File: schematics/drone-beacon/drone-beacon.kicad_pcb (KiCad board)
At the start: 2 copper layers, 23.3 x 29.9 mm, 13 parts, among them J1 ESP32 Flashing connector, J2 Power Input, SW1 Model selection, U1 ESP32-WROOM-32U, U2 AMS1117-3.3, U3 L80-R

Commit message: Update schematics
Signed-off-by: LAMBS Pierre-Antoine <pierreantoine.lambs@gmail.com>
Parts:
- C1, C2, C3, C4: footprint Capacitor_SMD:C_0201_0603Metric -> Capacitor_SMD:C_0402_1005Metric_Pad0.74x0.62mm_HandSolder
- D1: footprint LED_SMD:LED_0201_0603Metric -> LED_SMD:LED_0402_1005Metric_Pad0.77x0.64mm_HandSolder
- R1, R3: footprint Resistor_SMD:R_0201_0603Metric -> Resistor_SMD:R_0402_1005Metric_Pad0.72x0.64mm_HandSolder
- U3: value L80-R -> L96; footprint RF_GPS:Quectel_L96 -> QUECTEL_L96:L96
- moved D1 23.7 mm to (200.8, 51.9), turned to 90 degrees
- moved R1 21.7 mm to (200.8, 54.7), turned to 90 degrees
- moved R3 4.89 mm to (200.3, 72.5), turned to 0 degrees
- moved U3 0.42 mm to (190.8, 72.3)
- moved C2 0.21 mm to (190.8, 56.2)
- moved C3 0.13 mm to (196.9, 60.6)
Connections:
- U3 pad 1: /GPS_RX -> unconnected-(U3-NC1-Pad1)
- U3 pad 10: unconnected-(U3-~{RESET}-Pad10) -> GND
- U3 pad 11: unconnected-(U3-RESERVED-Pad11) -> GND
- U3 pad 13: (no net) -> GND
- U3 pad 14: (no net) -> GND
- U3 pad 15: (no net) -> GND
- U3 pad 16: (no net) -> unconnected-(U3-RF_OUT-Pad16)
- U3 pad 17: (no net) -> unconnected-(U3-RF_IN-Pad17)
- U3 pad 18: (no net) -> GND
- U3 pad 19: (no net) -> GND
- U3 pad 2: /GPS_TX -> unconnected-(U3-3D_FIX-Pad2)
- U3 pad 20: (no net) -> unconnected-(U3-JAM_DET-Pad20)
- U3 pad 21: (no net) -> GND
- U3 pad 22: (no net) -> GND
- U3 pad 23: (no net) -> +3.3V
- U3 pad 24: (no net) -> unconnected-(U3-GEO_FENCE-Pad24)
- U3 pad 25: (no net) -> /GPS_TX
- U3 pad 26: (no net) -> /GPS_RX
- U3 pad 27: (no net) -> GND
- U3 pad 28: (no net) -> unconnected-(U3-FORCE_ON-Pad28)
- U3 pad 29: (no net) -> /GPS_PPS
- U3 pad 3: GND -> unconnected-(U3-I2C_SDA-Pad3)
- U3 pad 30: (no net) -> unconnected-(U3-ANTON-Pad30)
- U3 pad 31: (no net) -> GND
- U3 pad 4: +3.3V -> GND
- U3 pad 5: unconnected-(U3-V_BCKP-Pad5) -> GND
- U3 pad 6: /GPS_PPS -> unconnected-(U3-I2C_SCL-Pad6)
- U3 pad 9: unconnected-(U3-NC-Pad9) -> +3.3V
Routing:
- net /GPS_PPS: track 18.3 -> 36.3 mm
- net +3.3V: track 51.3 -> 66.1 mm
- net /GPS_RX: track 13.4 -> 26.9 mm
- net /GPS_TX: track 14.6 -> 26.3 mm
- net /ESP32_EN: track 27.0 -> 32.3 mm
- net GND: track 4.50 -> 0.01 mm, vias 4 -> 3
- net /STATUS_LED: track 18.8 -> 21.4 mm
- net Net-(D1-K): track 0.80 -> 0.00 mm

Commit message: Update schematics (WIP)
Signed-off-by: LAMBS Pierre-Antoine <pierreantoine.lambs@gmail.com>
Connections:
- U1 pad 14: /DIP1 -> unconnected-(U1-IO12-Pad14)
- U1 pad 16: unconnected-(U1-IO13-Pad16) -> /DIP1
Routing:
- net /DIP1: track 21.9 -> 18.6 mm
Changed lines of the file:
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@@
 	(net 21 "unconnected-(U1-SHD{slash}SD2-Pad17)")
 	(net 22 "unconnected-(U1-IO33-Pad9)")
-	(net 23 "unconnected-(U1-IO13-Pad16)")
+	(net 23 "unconnected-(U1-IO12-Pad14)")
 	(net 24 "unconnected-(U1-IO18-Pad30)")
 	(net 25 "unconnected-(U1-IO5-Pad29)")
@@
 			(size 1.5 0.9)
 			(layers "F.Cu" "F.Mask" "F.Paste")
-			(net 10 "/DIP1")
+			(net 23 "unconnected-(U1-IO12-Pad14)")
 			(pinfunction "IO12")
-			(pintype "bidirectional")
+			(pintype "bidirectional+no_connect")
 		)
 		(pad "15" smd rect
@@
 			(size 1.5 0.9)
 			(layers "F.Cu" "F.Mask" "F.Paste")
-			(net 23 "unconnected-(U1-IO13-Pad16)")
+			(net 10 "/DIP1")
 			(pinfunction "IO13")
-			(pintype "bidirectional+no_connect")
+			(pintype "bidirectional")
 		)
 		(pad "17" smd rect
@@
 	)
 	(segment
-		(start 199.8 53.15)
-		(end 194.15 53.15)
+		(start 194.15 53.15)
+		(end 195.236 53.15)
+		(width 0.2)
+		(layer "F.Cu")
+		(net 10)
+	)
+	(segment
+		(start 195.236 53.15)
+		(end 195.495 52.891)
 		(width 0.2)
 		(layer "F.Cu")
@@
 		(width 0.2)
 		(layer "F.Cu")
+		(net 10)
+	)
+	(segment
+		(start 195.495 52.891)
+		(end 195.495 52.055)
+		(width 0.2)
+		(layer "F.Cu")

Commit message: Update schematics
Signed-off-by: LAMBS Pierre-Antoine <pierreantoine.lambs@gmail.com>
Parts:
- added R2: 0, Resistor_SMD:R_0402_1005Metric_Pad0.72x0.64mm_HandSolder, B.Cu at (181.3, 75.7)
- U3: footprint QUECTEL_L96:L96 -> RF_GPS:Quectel_L96
- moved SW1 15.5 mm to (198.4, 70.3), turned to 90 degrees
- moved J2 3.75 mm to (196.8, 77.5), turned to 90 degrees
- moved U3 2.87 mm to (187.9, 72.3), turned to 180 degrees
- moved J1 1.21 mm to (186.3, 54.3)
- moved U2 0.51 mm to (195.8, 54.5), turned to 180 degrees
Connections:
- C1 pad 1: Net-(J2-Pin_1) -> /VIN
- C2 pad 1: Net-(J2-Pin_1) -> /VIN
- J2 pad 1: Net-(J2-Pin_1) -> GND
- J2 pad 2: GND -> /VIN
- U2 pad 3: Net-(J2-Pin_1) -> /VIN
- U3 pad 16: unconnected-(U3-RF_OUT-Pad16) -> /RF_OUT
- U3 pad 17: unconnected-(U3-RF_IN-Pad17) -> /RF_IN
- U3 pad 8: unconnected-(U3-V_BCKP-Pad8) -> +3.3V
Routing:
- net +3.3V: track 66.1 -> 0.00 mm, vias 1 -> 0
- net /GPS_PPS: track 36.3 -> 0.00 mm, vias 1 -> 0
- net Net-(J2-Pin_1): track 32.6 -> 0.00 mm, vias 1 -> 0
- net /ESP32_EN: track 32.3 -> 0.00 mm, vias 1 -> 0
- net /DIP4: track 28.9 -> 0.00 mm, vias 1 -> 0
- net /GPS_RX: track 26.9 -> 0.00 mm, vias 1 -> 0
- net /DIP3: track 26.5 -> 0.00 mm, vias 1 -> 0
- net /GPS_TX: track 26.3 -> 0.00 mm, vias 1 -> 0
- net /DIP2: track 24.3 -> 0.00 mm, vias 1 -> 0
- net /STATUS_LED: track 21.4 -> 0.00 mm, vias 1 -> 0
- net /DIP1: track 18.6 -> 0.00 mm, vias 1 -> 0
- net /ESP32_TX: track 12.1 -> 0.00 mm, vias 1 -> 0
- net /ESP32_RX: track 10.9 -> 0.00 mm, vias 1 -> 0
- net /ESP32_BOOT: track 6.64 -> 0.00 mm, vias 1 -> 0
- net GND: track 0.01 -> 0.00 mm, vias 3 -> 0
- removed copper zone on B.Cu, net GND
- removed copper zone on F.Cu, net GND
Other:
- board size 23.3 x 29.9 mm -> 21.4 x 30.5 mm

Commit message: Update schematics v1
Signed-off-by: LAMBS Pierre-Antoine <pierreantoine.lambs@gmail.com>
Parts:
- J2, R3: moved to B.Cu
- R2: moved to F.Cu
- moved SW1 92.5 mm to (108.1, 50.5), turned to 0 degrees
- moved R3 88.2 mm to (113.4, 57.5), turned to 180 degrees
- moved D1 83.2 mm to (120.1, 71.8), turned to -90 degrees
- moved R1 82.1 mm to (120.0, 69.2), turned to -90 degrees
- moved U3 81.5 mm to (106.6, 67.5)
- moved U1 81.0 mm to (110.2, 57.3), turned to 0 degrees
- moved R2 80.5 mm to (101.1, 68.5), turned to 0 degrees
- moved C3 79.7 mm to (117.8, 69.6), turned to 180 degrees
- moved J2 79.3 mm to (117.6, 72.4)
- moved U2 79.2 mm to (117.1, 62.8), turned to 90 degrees
- moved C4 78.6 mm to (117.8, 68.6), turned to 180 degrees
- moved C1 77.5 mm to (115.3, 68.6), turned to 0 degrees
- moved C2 76.7 mm to (115.3, 69.6), turned to 0 degrees
- moved J1 69.2 mm to (117.2, 51.9), turned to -90 degrees
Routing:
- net +3.3V: track 0.00 -> 68.4 mm, vias 0 -> 1
- net /ESP32_EN: track 0.00 -> 30.2 mm, vias 0 -> 1
- net /ESP32_BOOT: track 0.00 -> 27.1 mm, vias 0 -> 1
- net /DIP4: track 0.00 -> 21.8 mm, vias 0 -> 1
- net /DIP3: track 0.00 -> 21.4 mm, vias 0 -> 1
- net /DIP2: track 0.00 -> 21.0 mm, vias 0 -> 1
- net GND: track 0.00 -> 20.3 mm, vias 0 -> 8
- net /DIP1: track 0.00 -> 19.6 mm, vias 0 -> 1
- net /GPS_RX: track 0.00 -> 18.2 mm, vias 0 -> 1
- net /GPS_TX: track 0.00 -> 17.4 mm, vias 0 -> 1
- net /GPS_PPS: track 0.00 -> 15.6 mm, vias 0 -> 1
- net /VIN: track 0.00 -> 6.80 mm
- net /ESP32_RX: track 0.00 -> 5.12 mm, vias 0 -> 1
- net /ESP32_TX: track 0.00 -> 5.03 mm, vias 0 -> 1
- net /RF_OUT: track 0.00 -> 4.99 mm, vias 0 -> 1
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- added copper zone on B.Cu, net GND
- added copper zone on F.Cu, net GND
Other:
- board size 21.4 x 30.5 mm -> 22.4 x 30 mm
- board text added: "V1"
- board text added: "github.com/plambs drone-beacon"
- board text removed: "Drone-beacon github.com/plambs"

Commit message: Update schematics
Signed-off-by: LAMBS Pierre-Antoine <pierreantoine.lambs@gmail.com>
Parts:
- added TP1: TestPoint, TestPoint:TestPoint_Pad_D1.0mm, F.Cu at (89.7, 77.6)
- added TP2: TestPoint, TestPoint:TestPoint_Pad_D1.0mm, F.Cu at (91.7, 77.6)
- added TP3: TestPoint, TestPoint:TestPoint_Pad_D1.0mm, F.Cu at (92.2, 84.5)
- added TP4: TestPoint, TestPoint:TestPoint_Pad_D1.0mm, F.Cu at (92.2, 82.5)
- added TP5: TestPoint, TestPoint:TestPoint_Pad_D1.0mm, F.Cu at (92.2, 86.5)
- added TP6: TestPoint, TestPoint:TestPoint_Pad_D1.0mm, F.Cu at (92.2, 88.6)
- added TP7: TestPoint, TestPoint:TestPoint_Pad_D1.0mm, F.Cu at (87.7, 77.6)
- added TP8: TestPoint, TestPoint:TestPoint_Pad_D1.0mm, F.Cu at (92.2, 80.5)
- C1, C2, C3, C4, D1, J1, J2, R1, R3, SW1, U2, U3: moved to F.Cu
- U1: moved to B.Cu
- moved SW1 34.5 mm to (98.5, 83.7), turned to 180 degrees
- moved R2 34.1 mm to (106.0, 102.2), turned to -90 degrees
- moved J1 33.0 mm to (91.2, 72.2), turned to 180 degrees
- moved U3 32.5 mm to (98.6, 98.9), turned to 0 degrees
- moved R3 30.3 mm to (89.2, 75.7)
- moved U1 24.4 mm to (98.6, 78.8), turned to 180 degrees
- moved C4 23.4 mm to (95.4, 75.3), turned to -90 degrees
- moved R1 22.9 mm to (97.2, 71.9), turned to 90 degrees
- moved D1 22.2 mm to (97.9, 70.0), turned to 0 degrees
- moved C3 21.9 mm to (96.6, 75.3), turned to -90 degrees
- moved U2 16.5 mm to (103.8, 72.7), turned to 0 degrees
- moved C1 9.26 mm to (109.4, 75.8), turned to -90 degrees
- moved J2 7.75 mm to (110.0, 70.8), turned to 0 degrees
- moved C2 7.72 mm to (110.6, 75.8), turned to -90 degrees
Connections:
- U3 pad 8: +3.3V -> unconnected-(U3-V_BCKP-Pad8)
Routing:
- net /DIP1: track 19.6 -> 2.88 mm
- net /DIP4: track 21.8 -> 5.63 mm
- net /DIP3: track 21.4 -> 5.63 mm
- net /DIP2: track 21.0 -> 5.63 mm
- net +3.3V: track 68.4 -> 83.7 mm, vias 1 -> 4
- net /STATUS_LED: track 4.96 -> 20.2 mm, vias 1 -> 2
- net /GPS_TX: track 17.4 -> 31.5 mm, vias 1 -> 2
- net /GPS_RX: track 18.2 -> 32.0 mm, vias 1 -> 2
- net /ESP32_BOOT: track 27.1 -> 18.7 mm, vias 1 -> 2
- net /ESP32_EN: track 30.2 -> 24.4 mm
- net /VIN: track 6.80 -> 12.5 mm
- net /GPS_PPS: track 15.6 -> 20.0 mm, vias 1 -> 2
- net GND: track 20.3 -> 24.5 mm, vias 8 -> 65
- net /RF_OUT: track 4.99 -> 2.52 mm, vias 1 -> 0
- net /ESP32_RX: track 5.12 -> 3.20 mm
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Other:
- board size 22.4 x 30 mm -> 26.8 x 37.3 mm
- board text removed: "V1"
- board text removed: "github.com/plambs drone-beacon"

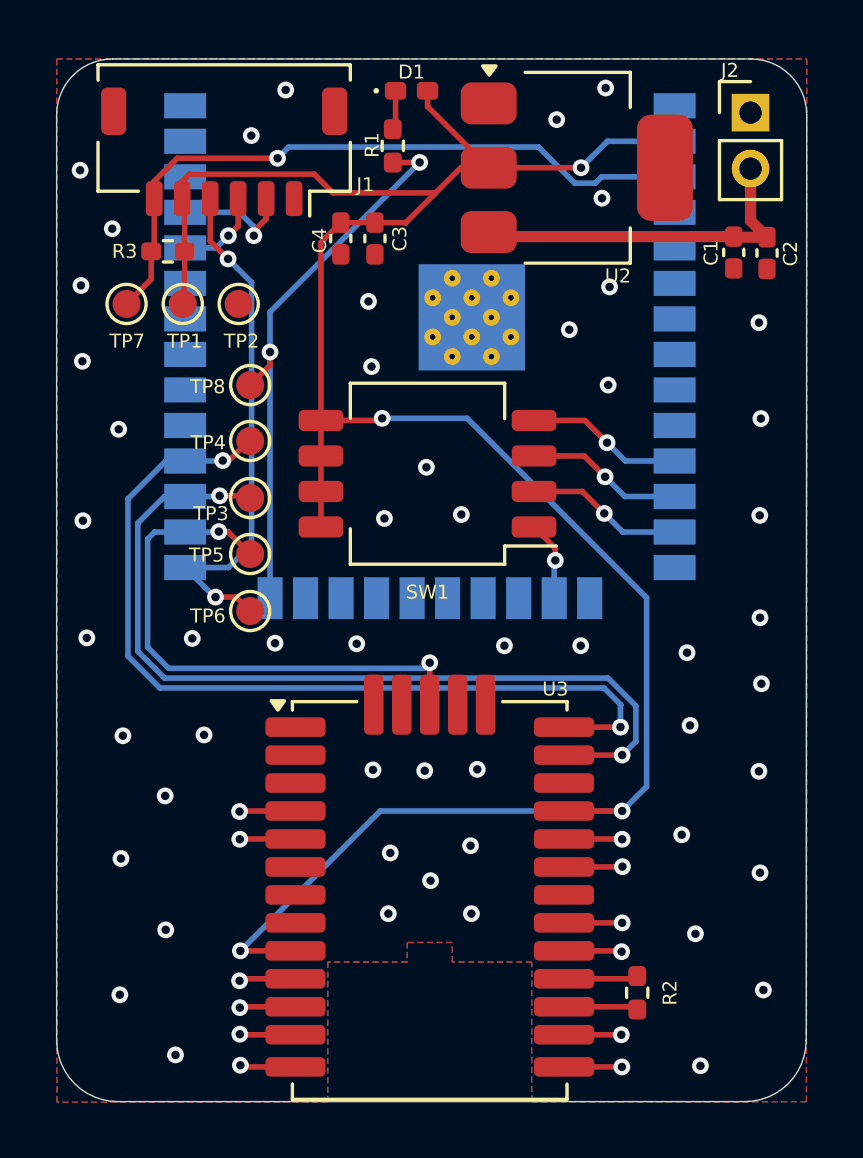
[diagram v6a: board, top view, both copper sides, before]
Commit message: schematics: update schematics and add missing pull up/down
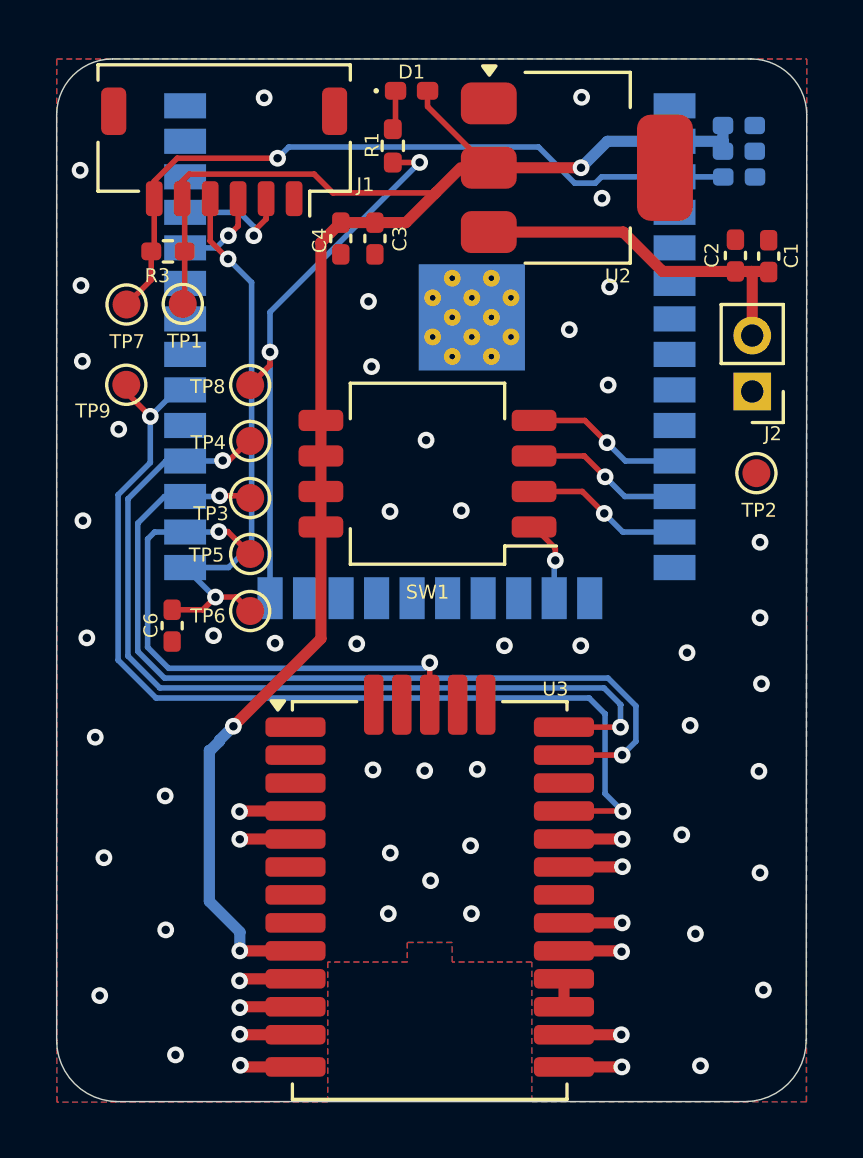
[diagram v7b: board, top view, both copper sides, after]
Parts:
- removed R2: 0, Resistor_SMD:R_0402_1005Metric_Pad0.72x0.64mm_HandSolder
- added C5: 0.1uF, Capacitor_SMD:C_0402_1005Metric_Pad0.74x0.62mm_HandSolder, B.Cu at (109.6, 73.1)
- added C6: 0.1uF, Capacitor_SMD:C_0402_1005Metric_Pad0.74x0.62mm_HandSolder, F.Cu at (89.4, 89.1)
- added C7: 0.1uF, Capacitor_SMD:C_0402_1005Metric_Pad0.74x0.62mm_HandSolder, B.Cu at (109.6, 71.2)
- added C8: 10uF, Capacitor_SMD:C_0402_1005Metric_Pad0.74x0.62mm_HandSolder, B.Cu at (109.6, 72.1)
- added TP9: TestPoint, TestPoint:TestPoint_Pad_D1.0mm, F.Cu at (87.7, 80.5)
- moved TP2 19.5 mm to (110.2, 83.7)
- moved J2 9.97 mm to (110.1, 80.7), turned to 180 degrees
- moved C1 1.26 mm to (110.7, 75.9), turned to 90 degrees
- moved C2 1.13 mm to (109.5, 75.9), turned to 90 degrees
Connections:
- U1 pad 30: unconnected-(U1-IO18-Pad30) -> /GPS_RESET
- U3 pad 16: /RF_OUT -> /RF_IN
- U3 pad 23: +3.3V -> /GPS_RESET
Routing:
- net /GPS_RESET: track 0.00 -> 36.4 mm, vias 0 -> 2
- net +3.3V: track 83.7 -> 64.5 mm, vias 4 -> 3
- net /RF_OUT: track 2.52 -> 0.00 mm
- net /ESP32_EN: track 24.4 -> 26.1 mm
- net /ESP32_BOOT: track 18.7 -> 20.4 mm
- net /RF_IN: track 2.52 -> 1.00 mm
- net GND: vias 65 -> 59
